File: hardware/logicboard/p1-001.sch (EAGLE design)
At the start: 23 parts, among them IC1 74LS07N, U1 TLC5940-NT

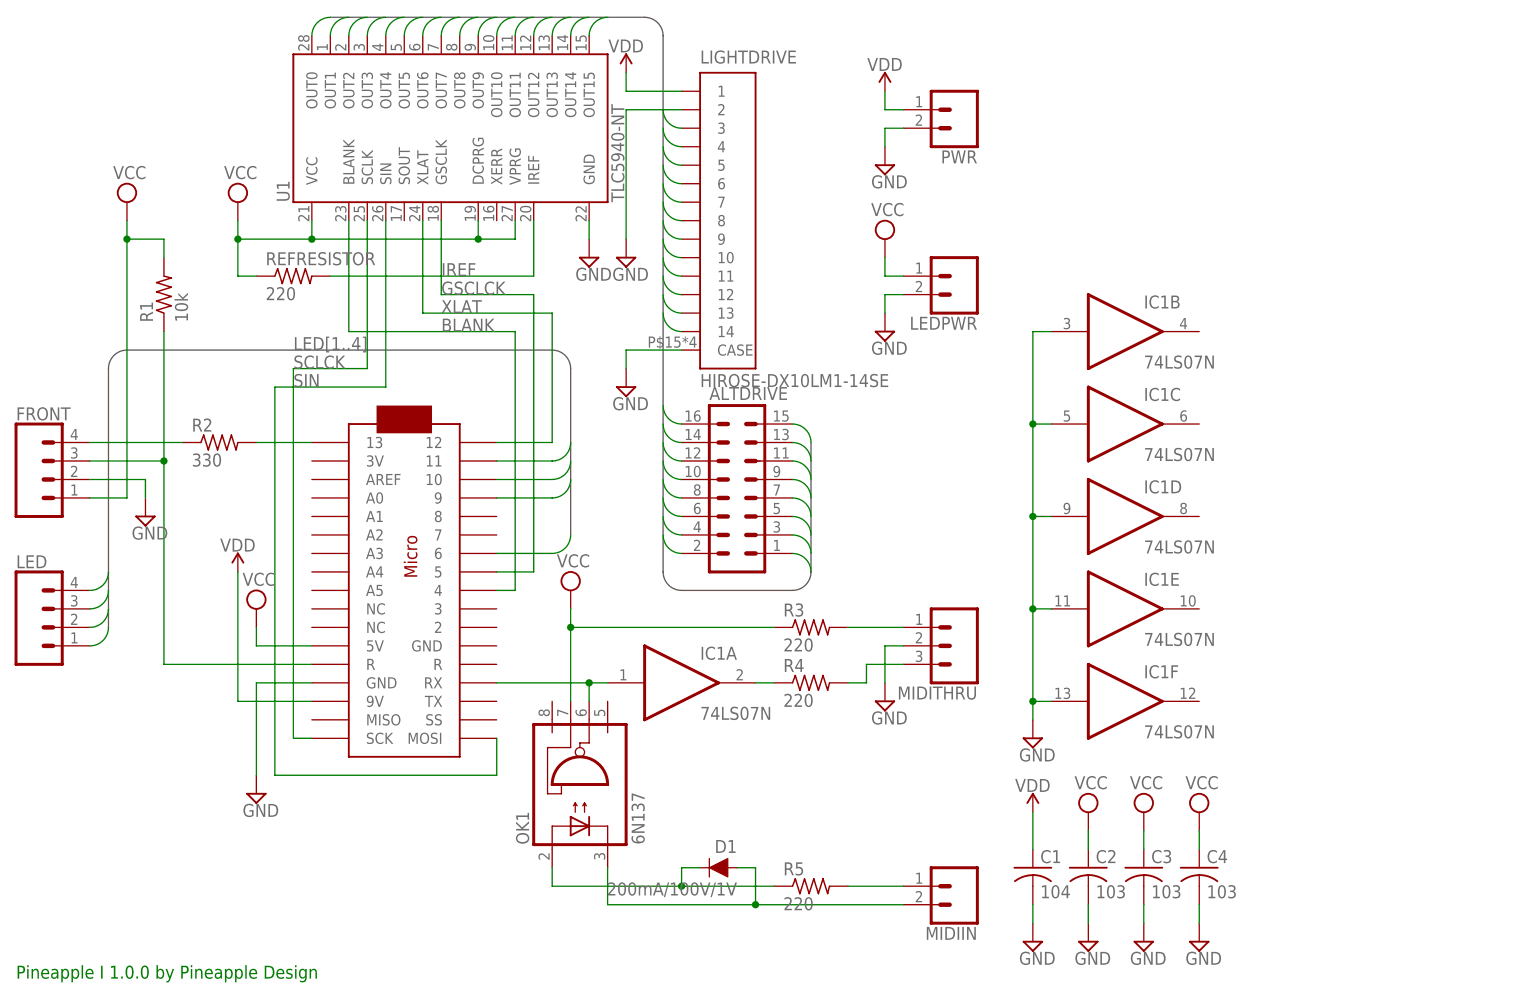
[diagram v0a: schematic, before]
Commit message: Fixed (missed) LED resistors.
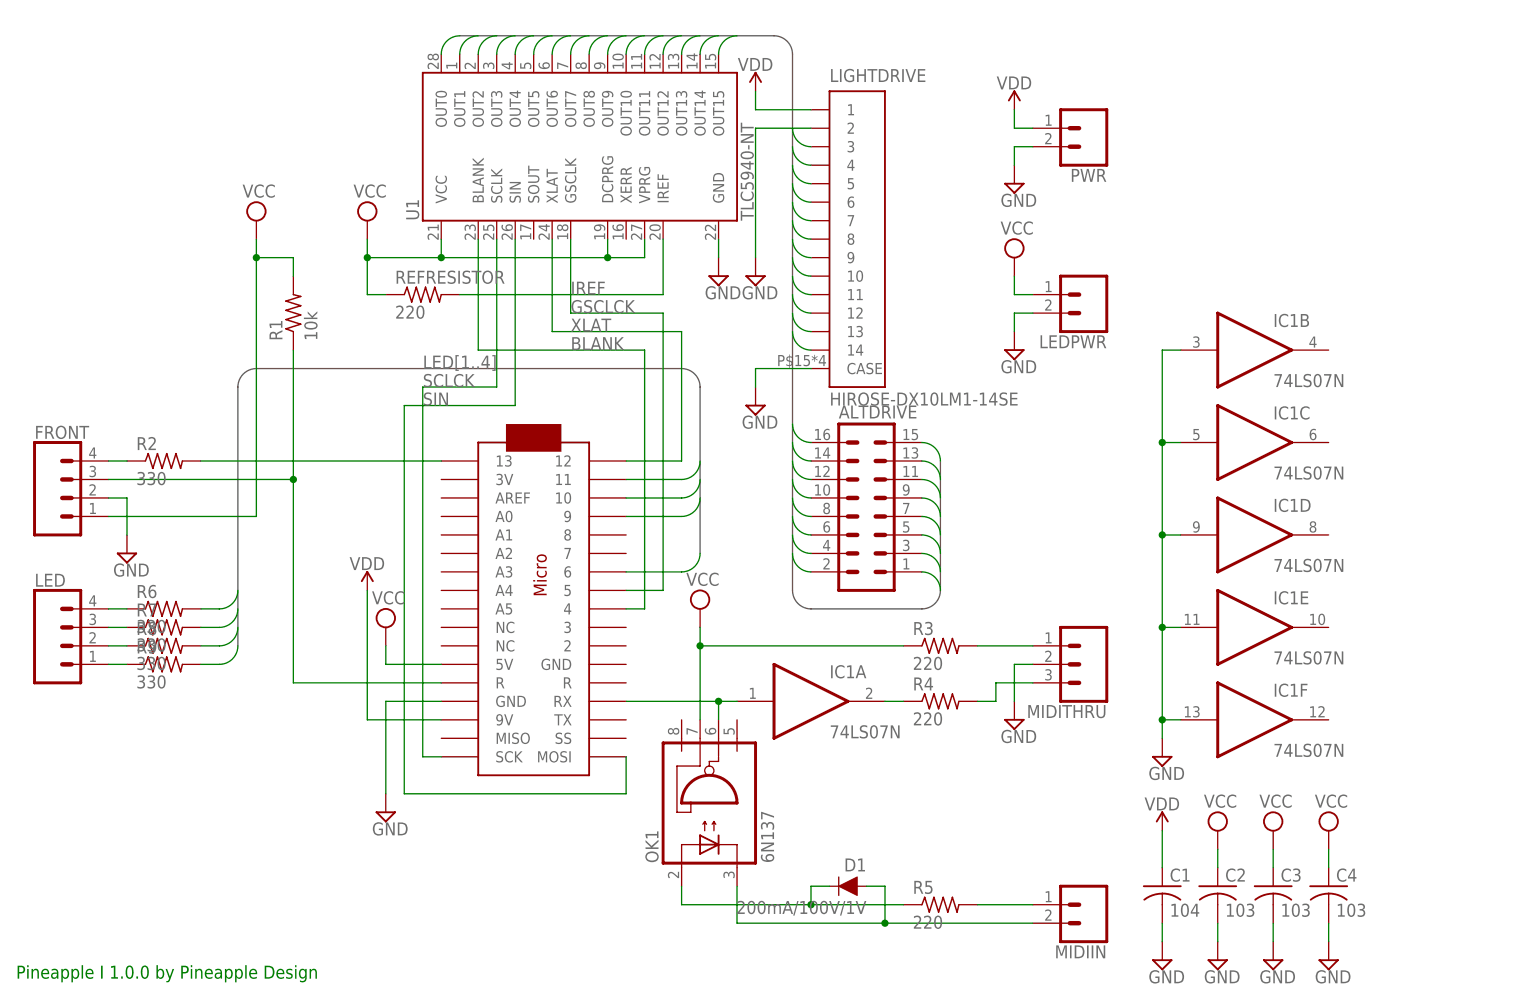
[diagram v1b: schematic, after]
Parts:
- added R6, R7, R8, R9: 330, resistor:R-US_0204/5
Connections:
- new net N$10: LED.3, R7.1
- new net N$12: LED.2, R8.1
- new net N$13: LED.1, R9.1
- new net N$7: LED.4, R6.1
- net LED1: now also R9.2; no longer LED.1
- net LED2: now also R8.2; no longer LED.2
- net LED3: now also R7.2; no longer LED.3
- net LED4: now also R6.2; no longer LED.4
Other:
- moved on the sheet: ALTDRIVE, C1, C2, C3, C4, D1, FRONT, IC1A, IC1B, IC1C, IC1D, IC1E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

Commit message: Moved AltDrive position and added new drill holes.
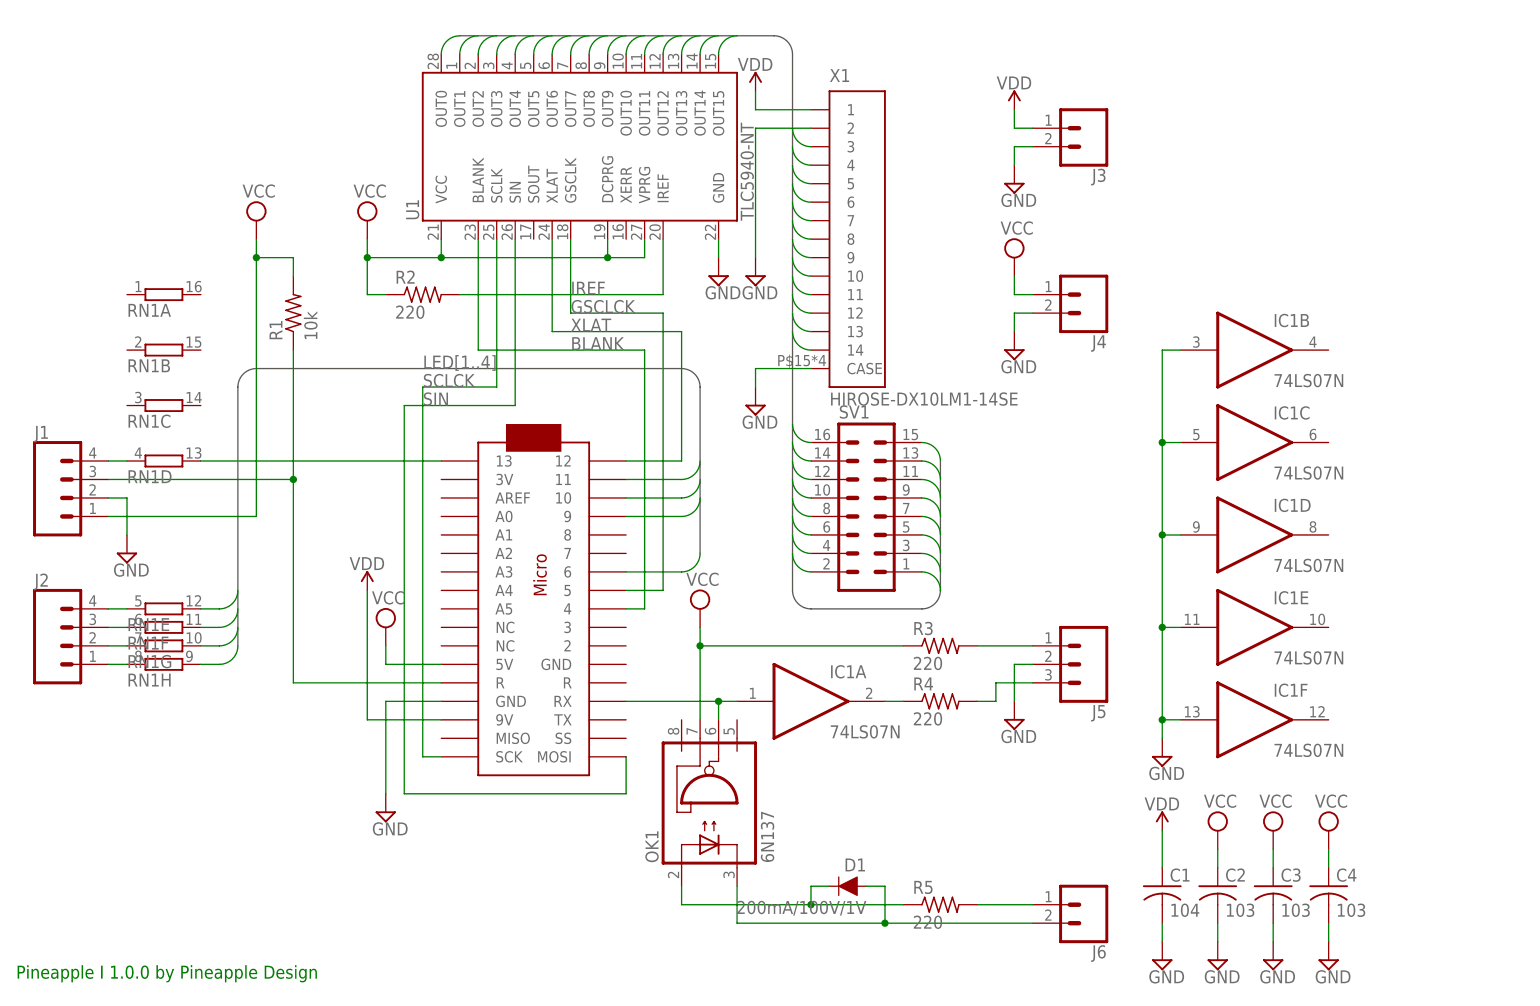
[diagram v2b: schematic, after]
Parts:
- removed R6, R7, R8, R9: 330, resistor:R-US_0204/5
- removed REFRESISTOR: 220, resistor:R-US_0204/5
- added RN1: (no value), resistor-dil:8R-N
- R2: value 330 -> 220
- renumbered ALTDRIVE to SV1, FRONT to J1, LED to J2, LEDPWR to J4, LIGHTDRIVE to X1, MC1 to U$1, MIDIIN to J6, MIDITHRU to J5, PWR to J3
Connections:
- net IREF: now also R2.2; no longer REFRESISTOR.2
- net LED1: now also RN1H.2; no longer R9.2
- net LED2: now also RN1G.2; no longer R8.2
- net LED3: now also RN1F.2; no longer R7.2
- net LED4: now also RN1E.2; no longer R6.2
- net N$10: now also RN1F.1; no longer R7.1
- net N$12: now also RN1G.1; no longer R8.1
- net N$13: now also RN1H.1; no longer R9.1
- net N$7: now also RN1E.1; no longer R6.1
- net N$8: now also RN1D.1; no longer R2.1
- net N$9: now also RN1D.2; no longer R2.2
- net VCC: now also R2.1; no longer REFRESISTOR.1
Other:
- moved on the sheet: R2

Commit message: Update silk.
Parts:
- renumbered J1 to FRONT, J2 to LED, J3 to PWR12V, J4 to LEDPWR, J5 to MIDIOUT, J6 to MIDIIN
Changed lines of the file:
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@@
 <part name="SUPPLY5" library="supply2" library_urn="urn:adsk.eagle:library:372" deviceset="VCC" device=""/>
 <part name="SUPPLY6" library="supply2" library_urn="urn:adsk.eagle:library:372" deviceset="GND" device=""/>
-<part name="J6" library="SparkFun-Connectors" deviceset="CONN_02" device="-JST-2-PTH-NO_SILK"/>
-<part name="J5" library="SparkFun-Connectors" deviceset="CONN_03" device="JST-PTH"/>
+<part name="MIDIIN" library="SparkFun-Connectors" deviceset="CONN_02" device="-JST-2-PTH-NO_SILK"/>
+<part name="MIDIOUT" library="SparkFun-Connectors" deviceset="CONN_03" device="JST-PTH"/>
 <part name="SUPPLY16" library="supply2" library_urn="urn:adsk.eagle:library:372" deviceset="GND" device=""/>
 <part name="U1" library="SparkFun-Retired" deviceset="TLC5940" device="-NT"/>
 <part name="SUPPLY3" library="supply2" library_urn="urn:adsk.eagle:library:372" deviceset="VCC" device=""/>
 <part name="SUPPLY8" library="supply2" library_urn="urn:adsk.eagle:library:372" deviceset="GND" device=""/>
-<part name="J3" library="SparkFun-Connectors" deviceset="CONN_02" device="-JST-2-PTH-NO_SILK"/>
+<part name="PWR12V" library="SparkFun-Connectors" deviceset="CONN_02" device="-JST-2-PTH-NO_SILK"/>
 <part name="SUPPLY12" library="SparkFun-PowerSymbols" deviceset="VDD" device=""/>
 <part name="SUPPLY4" library="SparkFun-PowerSymbols" deviceset="VDD" device=""/>
 <part name="SUPPLY13" library="supply2" library_urn="urn:adsk.eagle:library:372" deviceset="GND" device=""/>
 <part name="SUPPLY10" library="supply2" library_urn="urn:adsk.eagle:library:372" deviceset="GND" device=""/>
-<part name="J1" library="SparkFun-Connectors" deviceset="CONN_04" device="JST-PTH"/>
+<part name="FRONT" library="SparkFun-Connectors" deviceset="CONN_04" device="JST-PTH"/>
 <part name="SUPPLY2" library="supply2" library_urn="urn:adsk.eagle:library:372" deviceset="VCC" device=""/>
 <part name="SUPPLY1" library="supply2" library_urn="urn:adsk.eagle:library:372" deviceset="GND" device=""/>
@@
 <part name="SUPPLY11" library="supply2" library_urn="urn:adsk.eagle:library:372" deviceset="GND" device=""/>
 <part name="SUPPLY18" library="SparkFun-PowerSymbols" deviceset="VDD" device=""/>
-<part name="J4" library="SparkFun-Connectors" deviceset="CONN_02" device="JST-PTH-2"/>
+<part name="LEDPWR" library="SparkFun-Connectors" deviceset="CONN_02" device="JST-PTH-2"/>
 <part name="SUPPLY14" library="supply2" library_urn="urn:adsk.eagle:library:372" deviceset="VCC" device=""/>
 <part name="SUPPLY15" library="supply2" library_urn="urn:adsk.eagle:library:372" deviceset="GND" device=""/>
 <part name="SV1" library="con-ml" library_urn="urn:adsk.eagle:library:164" deviceset="ML16L" device="" package3d_urn="urn:adsk.eagle:package:8682/1"/>
 <part name="R2" library="resistor" library_urn="urn:adsk.eagle:library:348" deviceset="R-US_" device="0204/5" package3d_urn="urn:adsk.eagle:package:25955/1" value="220"/>
-<part name="J2" library="SparkFun-Connectors" deviceset="CONN_04" device="JST-PTH"/>
+<part name="LED" library="SparkFun-Connectors" deviceset="CONN_04" device="JST-PTH"/>
 <part name="RN1" library="resistor-dil" library_urn="urn:adsk.eagle:library:342" deviceset="8R-N" device="" package3d_urn="urn:adsk.eagle:package:24913/1"/>
 <part name="U$1" library="adafruit" deviceset="ARDUINOMICRO" device=""/>
@@
 <instance part="SUPPLY5" gate="G$1" x="50.8" y="48.26"/>
 <instance part="SUPPLY6" gate="GND" x="50.8" y="22.86"/>
-<instance part="J6" gate="G$1" x="147.32" y="10.16" rot="R180"/>
-<instance part="J5" gate="J$1" x="147.32" y="43.18" rot="R180"/>
+<instance part="MIDIIN" gate="G$1" x="147.32" y="10.16" rot="R180"/>
+<instance part="MIDIOUT" gate="J$1" x="147.32" y="43.18" rot="R180"/>
 <instance part="SUPPLY16" gate="GND" x="137.16" y="35.56"/>
 <instance part="U1" gate="G$1" x="76.2" y="114.3" rot="R90"/>
 <instance part="SUPPLY3" gate="G$1" x="48.26" y="104.14"/>
 <instance part="SUPPLY8" gate="GND" x="96.52" y="96.52"/>
-<instance part="J3" gate="G$1" x="147.32" y="116.84" rot="R180"/>
+<instance part="PWR12V" gate="G$1" x="147.32" y="116.84" rot="R180"/>
 <instance part="SUPPLY12" gate="VDD" x="137.16" y="119.38"/>
 <instance part="SUPPLY4" gate="VDD" x="48.26" y="53.34"/>
 <instance part="SUPPLY13" gate="GND" x="137.16" y="109.22"/>
 <instance part="SUPPLY10" gate="GND" x="101.6" y="96.52"/>
-<instance part="J1" gate="G$1" x="7.62" y="66.04"/>
+<instance part="FRONT" gate="G$1" x="7.62" y="66.04"/>
 <instance part="SUPPLY2" gate="G$1" x="33.02" y="104.14"/>
 <instance part="SUPPLY1" gate="GND" x="15.24" y="58.42"/>
@@
 <instance part="SUPPLY11" gate="GND" x="101.6" y="78.74"/>
 <instance part="SUPPLY18" gate="VDD" x="157.48" y="20.32"/>
-<instance part="J4" gate="G$1" x="147.32" y="93.98" rot="R180"/>
+<instance part="LEDPWR" gate="G$1" x="147.32" y="93.98" rot="R180"/>
 <instance part="SUPPLY14" gate="G$1" x="137.16" y="99.06"/>
 <instance part="SUPPLY15" gate="GND" x="137.16" y="86.36"/>
 <instance part="SV1" gate="1" x="116.84" y="66.04"/>
 <instance part="R2" gate="G$1" x="55.88" y="93.98"/>
-<instance part="J2" gate="G$1" x="7.62" y="45.72"/>
+<instance part="LED" gate="G$1" x="7.62" y="45.72"/>
 <instance part="RN1" gate="A" x="20.32" y="93.98"/>
 <instance part="RN1" gate="B" x="20.32" y="86.36"/>
@@
 </segment>
 <segment>
-<pinref part="J5" gate="J$1" pin="2"/>
+<pinref part="MIDIOUT" gate="J$1" pin="2"/>
 <pinref part="SUPPLY16" gate="GND" pin="GND"/>
 <wire x1="139.7" y1="43.18" x2="137.16" y2="43.18" width="0.1524" layer="91"/>
@@
 </segment>
 <segment>
-<pinref part="J3" gate="G$1" pin="2"/>
+<pinref part="PWR12V" gate="G$1" pin="2"/>
 <wire x1="139.7" y1="114.3" x2="137.16" y2="114.3" width="0.1524" layer="91"/>
 <pinref part="SUPPLY13" gate="GND" pin="GND"/>
@@
 </segment>
 <segment>
-<pinref part="J1" gate="G$1" pin="2"/>
+<pinref part="FRONT" gate="G$1" pin="2"/>
 <wire x1="12.7" y1="66.04" x2="15.24" y2="66.04" width="0.1524" layer="91"/>
 <pinref part="SUPPLY1" gate="GND" pin="GND"/>
@@
 </segment>
 <segment>
-<pinref part="J4" gate="G$1" pin="2"/>
+<pinref part="LEDPWR" gate="G$1" pin="2"/>
 <wire x1="139.7" y1="91.44" x2="137.16" y2="91.44" width="0.1524" layer="91"/>
 <pinref part="SUPPLY15" gate="GND" pin="GND"/>
@@
 </segment>
 <segment>
-<pinref part="J1" gate="G$1" pin="1"/>
+<pinref part="FRONT" gate="G$1" pin="1"/>
 <wire x1="12.7" y1="63.5" x2="33.02" y2="63.5" width="0.1524" layer="91"/>
 <pinref part="SUPPLY2" gate="G$1" pin="VCC"/>
@@
 <pinref part="SUPPLY14" gate="G$1" pin="VCC"/>
 <wire x1="137.16" y1="96.52" x2="137.16" y2="93.98" width="0.1524" layer="91"/>
-<pinref part="J4" gate="G$1" pin="1"/>
+<pinref part="LEDPWR" gate="G$1" pin="1"/>
 <wire x1="137.16" y1="93.98" x2="139.7" y2="93.98" width="0.1524" layer="91"/>
 </segment>
@@
 <pinref part="R4" gate="G$1" pin="2"/>
 <wire x1="132.08" y1="38.1" x2="134.62" y2="38.1" width="0.1524" layer="91"/>
-<pinref part="J5" gate="J$1" pin="3"/>
+<pinref part="MIDIOUT" gate="J$1" pin="3"/>
 <wire x1="139.7" y1="40.64" x2="134.62" y2="40.64" width="0.1524" layer="91"/>
 <wire x1="134.62" y1="40.64" x2="134.62" y2="38.1" width="0.1524" layer="91"/>
@@
 <wire x1="119.38" y1="12.7" x2="119.38" y2="7.62" width="0.1524" layer="91"/>
 <junction x="119.38" y="7.62"/>
-<pinref part="J6" gate="G$1" pin="2"/>
+<pinref part="MIDIIN" gate="G$1" pin="2"/>
 </segment>
 </net>
@@
 <pinref part="R3" gate="G$1" pin="2"/>
 <wire x1="132.08" y1="45.72" x2="139.7" y2="45.72" width="0.1524" layer="91"/>
-<pinref part="J5" gate="J$1" pin="1"/>
+<pinref part="MIDIOUT" gate="J$1" pin="1"/>
 </segment>
 </net>
@@
 <pinref part="R5" gate="G$1" pin="2"/>
 <wire x1="132.08" y1="10.16" x2="139.7" y2="10.16" width="0.1524" layer="91"/>
-<pinref part="J6" gate="G$1" pin="1"/>
+<pinref part="MIDIIN" gate="G$1" pin="1"/>
 </segment>
 </net>
@@
 <pinref part="SUPPLY12" gate="VDD" pin="VDD"/>
 <wire x1="137.16" y1="119.38" x2="137.16" y2="116.84" width="0.1524" layer="91"/>
-<pinref part="J3" gate="G$1" pin="1"/>
+<pinref part="PWR12V" gate="G$1" pin="1"/>
 <wire x1="137.16" y1="116.84" x2="139.7" y2="116.84" width="0.1524" layer="91"/>
 </segment>
@@
 <net name="N$11" class="0">
 <segment>
-<pinref part="J1" gate="G$1" pin="3"/>
+<pinref part="FRONT" gate="G$1" pin="3"/>
 <wire x1="12.7" y1="68.58" x2="38.1" y2="68.58" width="0.1524" layer="91"/>
 <pinref part="R1" gate="G$1" pin="1"/>
@@
 <net name="N$8" class="0">
 <segment>
-<pinref part="J1" gate="G$1" pin="4"/>
+<pinref part="FRONT" gate="G$1" pin="4"/>
 <wire x1="12.7" y1="71.12" x2="15.24" y2="71.12" width="0.1524" layer="91"/>
 <pinref part="RN1" gate="D" pin="1"/>
@@
 <net name="N$7" class="0">
 <segment>
-<pinref part="J2" gate="G$1" pin="4"/>
+<pinref part="LED" gate="G$1" pin="4"/>
 <wire x1="15.24" y1="50.8" x2="12.7" y2="50.8" width="0.1524" layer="91"/>
 <pinref part="RN1" gate="E" pin="1"/>
@@
 <net name="N$10" class="0">
 <segment>
-<pinref part="J2" gate="G$1" pin="3"/>
+<pinref part="LED" gate="G$1" pin="3"/>
 <wire x1="15.24" y1="48.26" x2="12.7" y2="48.26" width="0.1524" layer="91"/>
 <pinref part="RN1" gate="F" pin="1"/>
@@
 <net name="N$12" class="0">
 <segment>
-<pinref part="J2" gate="G$1" pin="2"/>
+<pinref part="LED" gate="G$1" pin="2"/>
 <wire x1="15.24" y1="45.72" x2="12.7" y2="45.72" width="0.1524" layer="91"/>
 <pinref part="RN1" gate="G" pin="1"/>
@@
 <net name="N$13" class="0">
 <segment>
-<pinref part="J2" gate="G$1" pin="1"/>
+<pinref part="LED" gate="G$1" pin="1"/>
 <wire x1="15.24" y1="43.18" x2="12.7" y2="43.18" width="0.1524" layer="91"/>
 <pinref part="RN1" gate="H" pin="1"/>

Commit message: Fixed missing silk pattern.
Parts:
- MIDIIN, PWR12V: device SparkFun-Connectors:CONN_02-JST-2-PTH-NO_SILK -> SparkFun-Connectors:CONN_02JST-PTH-2
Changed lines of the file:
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@@
 <part name="SUPPLY5" library="supply2" library_urn="urn:adsk.eagle:library:372" deviceset="VCC" device=""/>
 <part name="SUPPLY6" library="supply2" library_urn="urn:adsk.eagle:library:372" deviceset="GND" device=""/>
-<part name="MIDIIN" library="SparkFun-Connectors" deviceset="CONN_02" device="-JST-2-PTH-NO_SILK"/>
+<part name="MIDIIN" library="SparkFun-Connectors" deviceset="CONN_02" device="JST-PTH-2"/>
 <part name="MIDIOUT" library="SparkFun-Connectors" deviceset="CONN_03" device="JST-PTH"/>
 <part name="SUPPLY16" library="supply2" library_urn="urn:adsk.eagle:library:372" deviceset="GND" device=""/>
@@
 <part name="SUPPLY3" library="supply2" library_urn="urn:adsk.eagle:library:372" deviceset="VCC" device=""/>
 <part name="SUPPLY8" library="supply2" library_urn="urn:adsk.eagle:library:372" deviceset="GND" device=""/>
-<part name="PWR12V" library="SparkFun-Connectors" deviceset="CONN_02" device="-JST-2-PTH-NO_SILK"/>
+<part name="PWR12V" library="SparkFun-Connectors" deviceset="CONN_02" device="JST-PTH-2"/>
 <part name="SUPPLY12" library="SparkFun-PowerSymbols" deviceset="VDD" device=""/>
 <part name="SUPPLY4" library="SparkFun-PowerSymbols" deviceset="VDD" device=""/>
